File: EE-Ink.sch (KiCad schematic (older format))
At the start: 76 parts

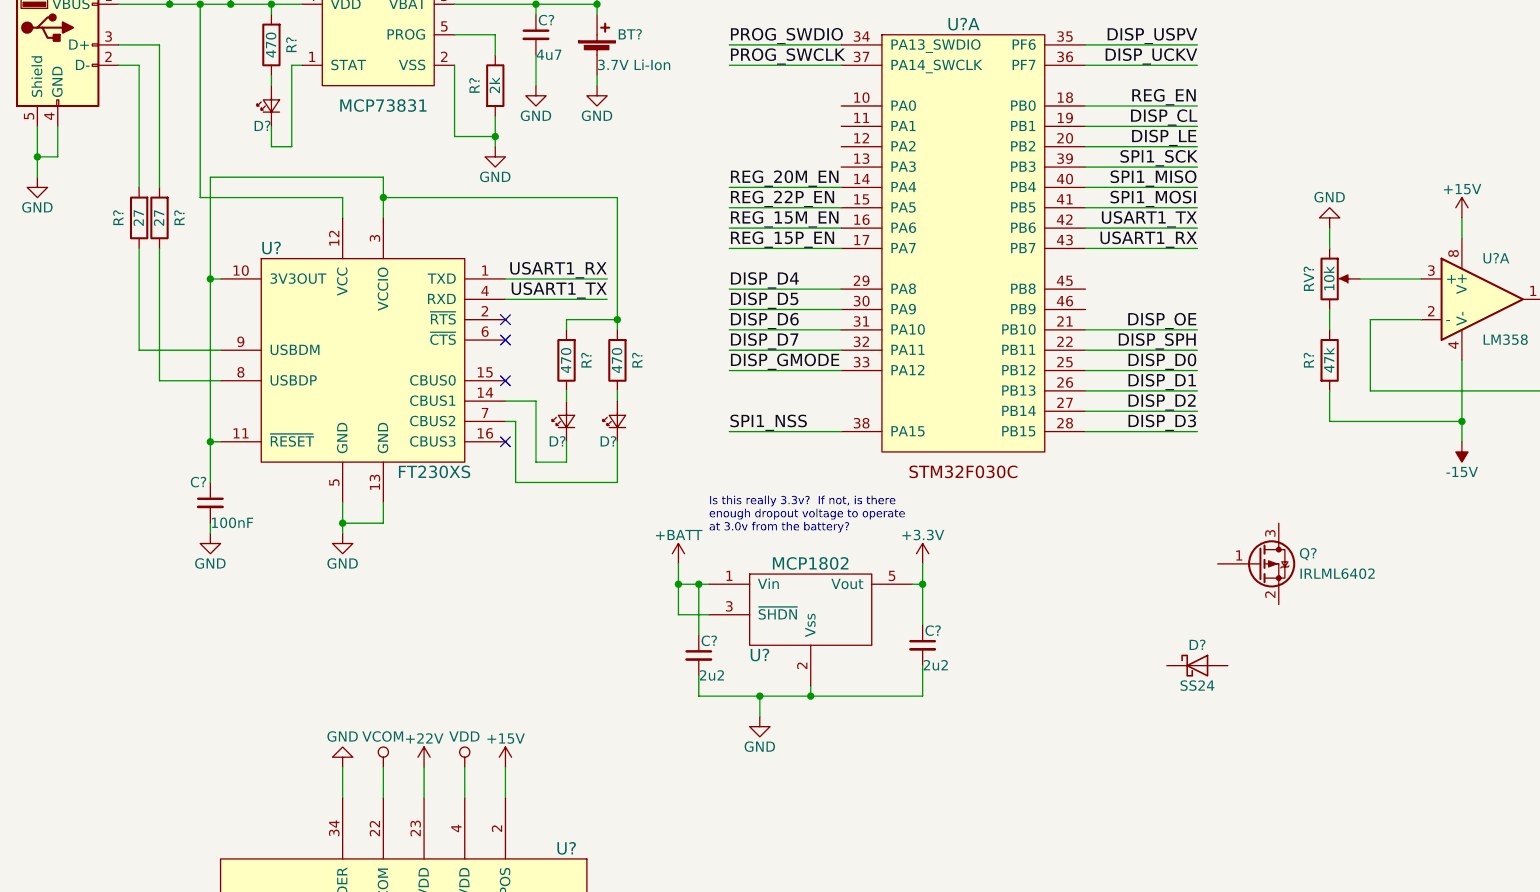
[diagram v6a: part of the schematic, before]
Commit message: Added battery voltage measuring.
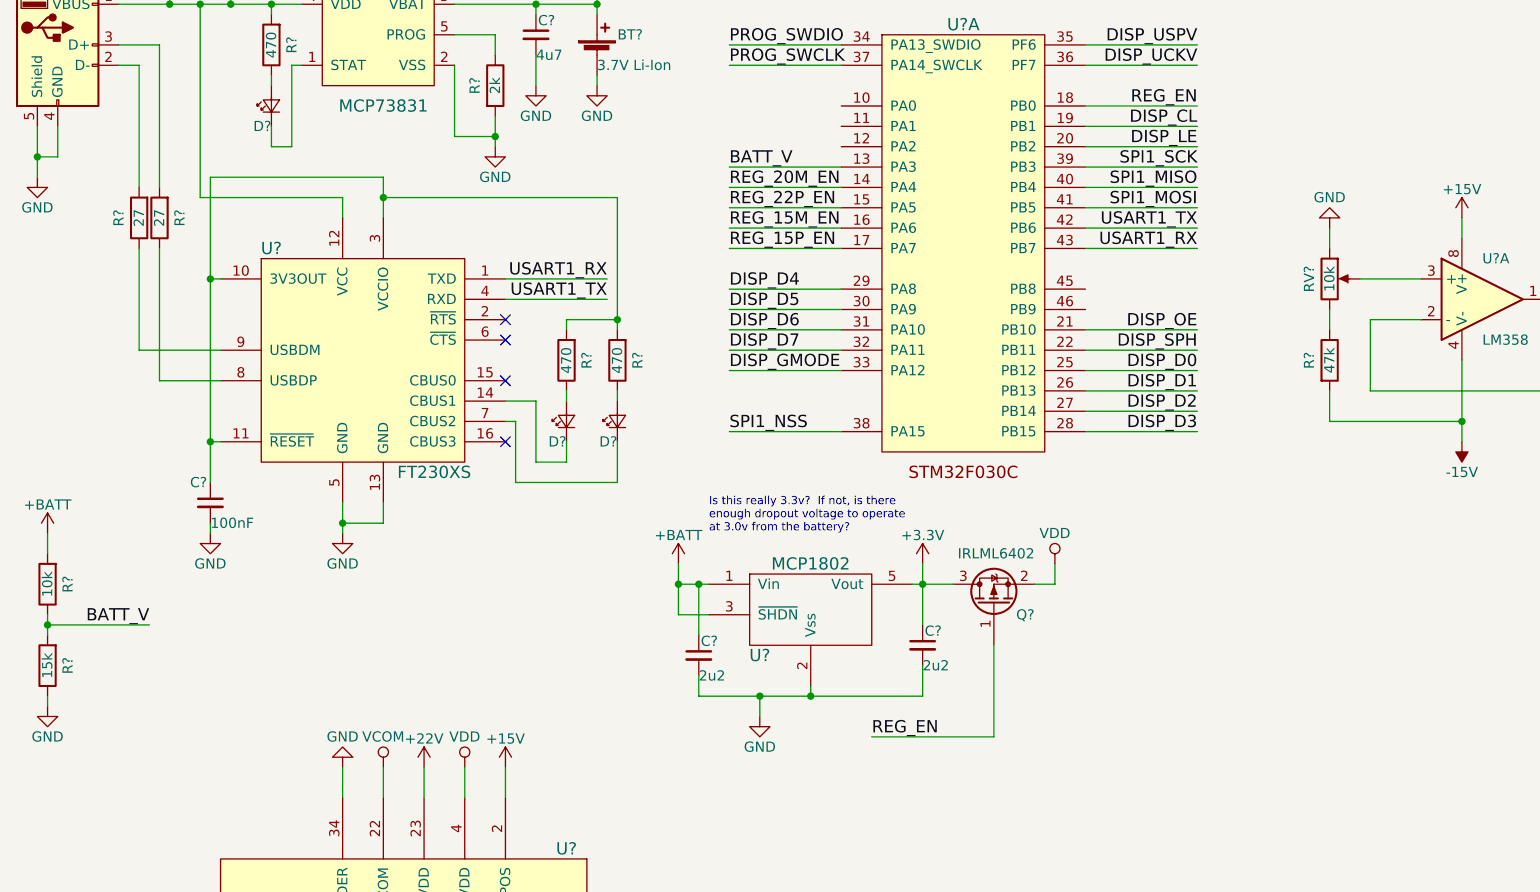
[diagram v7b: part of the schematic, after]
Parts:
- removed D?: SS24, symbol D_Schottky
- added R?: 15k, symbol R
- added R?: 10k, symbol R
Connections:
- net +3V3: now also Q?.3 (D)
- net +BATT: now also R?.2
- net GND: now also R?.1
- net REG_EN: now also Q?.1 (G)
- net VDD: now also Q?.2 (S)
- net BATT_V: now reaches U?.13 (PA3)
- net BATT_V: now also R?.1, R?.2
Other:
- moved on the sheet: Q?
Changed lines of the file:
@@
 L Q_PMOS_GSD Q?
 U 1 1 58D82351
-P 6650 3750
-F 0 "Q?" H 6850 3800 50  0000 L CNN
-F 1 "IRLML6402" H 6850 3700 50  0000 L CNN
-F 2 "" H 6850 3850 50  0001 C CNN
-F 3 "" H 6650 3750 50  0001 C CNN
-	1    6650 3750
-	1    0    0    -1
-$EndComp
-$Comp
-L D_Schottky D?
-U 1 1 58D829F1
-P 6350 4250
-F 0 "D?" H 6350 4350 50  0000 C CNN
-F 1 "SS24" H 6350 4150 50  0000 C CNN
-F 2 "" H 6350 4250 50  0001 C CNN
-F 3 "" H 6350 4250 50  0001 C CNN
-	1    6350 4250
-	1    0    0    -1
+P 5350 3950
+F 0 "Q?" V 5300 3750 50  0000 L CNN
+F 1 "IRLML6402" V 5600 3750 50  0000 L CNN
+F 2 "" H 5550 4050 50  0001 C CNN
+F 3 "" H 5350 3950 50  0001 C CNN
+	1    5350 3950
+	0    -1   -1   0
 $EndComp
 $Comp
@@
 	5000 3750 5000 4050
 Wire Wire Line
-	5000 3850 4950 3850
+	4950 3850 5150 3850
 Wire Wire Line
 	5000 4400 5000 4250
@@
 Text Label 4050 2200 0    60   ~ 0
 REG_15P_EN
+$Comp
+L VDD #PWR?
+U 1 1 58E887E4
+P 5650 3750
+F 0 "#PWR?" H 5650 3600 50  0001 C CNN
+F 1 "VDD" H 5650 3900 50  0000 C CNN
+F 2 "" H 5650 3750 50  0001 C CNN
+F 3 "" H 5650 3750 50  0001 C CNN
+	1    5650 3750
+	1    0    0    -1
+$EndComp
+Wire Wire Line
+	5650 3750 5650 3850
+Wire Wire Line
+	5650 3850 5550 3850
+Wire Wire Line
+	5350 4150 5350 4600
+Wire Wire Line
+	5350 4600 4750 4600
+Text Label 4750 4600 0    60   ~ 0
+REG_EN
+$Comp
+L +BATT #PWR?
+U 1 1 58E981DF
+P 700 3600
+F 0 "#PWR?" H 700 3450 50  0001 C CNN
+F 1 "+BATT" H 700 3740 50  0000 C CNN
+F 2 "" H 700 3600 50  0001 C CNN
+F 3 "" H 700 3600 50  0001 C CNN
+	1    700  3600
+	1    0    0    -1
+$EndComp
+$Comp
+L R R?
+U 1 1 58E983B7
+P 700 4250
+F 0 "R?" V 600 4250 50  0000 C CNN
+F 1 "15k" V 700 4250 50  0000 C CNN
+F 2 "" V 630 4250 50  0001 C CNN
+F 3 "" H 700 4250 50  0001 C CNN
+	1    700  4250
+	-1   0    0    1
+$EndComp
+$Comp
+L GND #PWR?
+U 1 1 58E9852D
+P 700 4450
+F 0 "#PWR?" H 700 4200 50  0001 C CNN
+F 1 "GND" H 700 4300 50  0000 C CNN
+F 2 "" H 700 4450 50  0001 C CNN
+F 3 "" H 700 4450 50  0001 C CNN
+	1    700  4450
+	1    0    0    -1
+$EndComp
+$Comp
+L R R?
+U 1 1 58E98765
+P 700 3850
+F 0 "R?" V 600 3850 50  0000 C CNN
+F 1 "10k" V 700 3850 50  0000 C CNN
+F 2 "" V 630 3850 50  0001 C CNN
+F 3 "" H 700 3850 50  0001 C CNN
+	1    700  3850
+	-1   0    0    1
+$EndComp
+Wire Wire Line
+	700  4450 700  4400
+Wire Wire Line
+	700  4100 700  4000
+Wire Wire Line
+	700  3700 700  3600
+Wire Wire Line
+	700  4050 1200 4050
+Connection ~ 700  4050
+Text Label 1200 4050 2    60   ~ 0
+BATT_V
+Text Label 4050 1800 0    60   ~ 0
+BATT_V
+Wire Wire Line
+	4600 1800 4050 1800
 $EndSCHEMATC

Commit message: Wired up power inputs for the mcu.
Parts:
- added C?: 0.01uF, symbol C_Small
- added C?: 1uF, symbol C_Small
- added C? (x2): 0.1uF, symbol C_Small
- added C?: 4.7uF, symbol C_Small
- added D?: LED_Small, symbol LED_Small
- added R?: 470, symbol R
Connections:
- net +3V3: now also U?.1 (VDD), U?.24 (VDD), U?.48 (VDD), U?.9 (VDDA), C?.1, C?.1, C?.1, C?.1, C?.1, C?.2, C?.2, C?.2, C?.2
- net GND: now also U?.23 (VSS), U?.47 (VSS), U?.8 (VSSA), C?.2, D?.1 (K)
- net LED_STATUS: now reaches U?.10 (PA0)
- net LED_STATUS: now also R?.2
- new net: D?.2 (A), R?.1
- no-connect marks 4 -> 17
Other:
- moved on the sheet: J?, U?B
